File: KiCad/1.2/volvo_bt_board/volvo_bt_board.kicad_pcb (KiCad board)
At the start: 2 copper layers, 109.2 x 94 mm, 19 parts, among them J1 DB9_Male, J10 A_RX, J11 A_TX, J12 A_RST, J2 DAC_B, J3 DAC_A, J4 SF0, J5 SF1, J6 12V, J7 GND, J8 GND, J9 5V, U1 ESP32-DEVKITC-32D

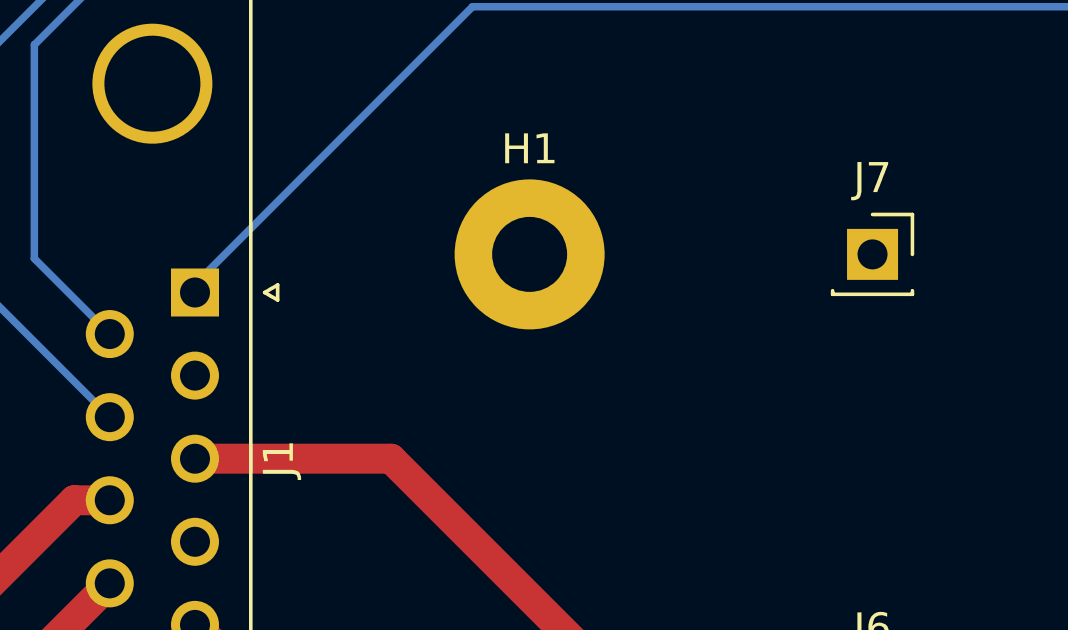
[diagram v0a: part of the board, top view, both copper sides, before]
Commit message: Add support for fast forward and reverse
 - Add support for scanmode (not tested)
 - Add ack bytes for approriate commands
 - Add board version 1.2
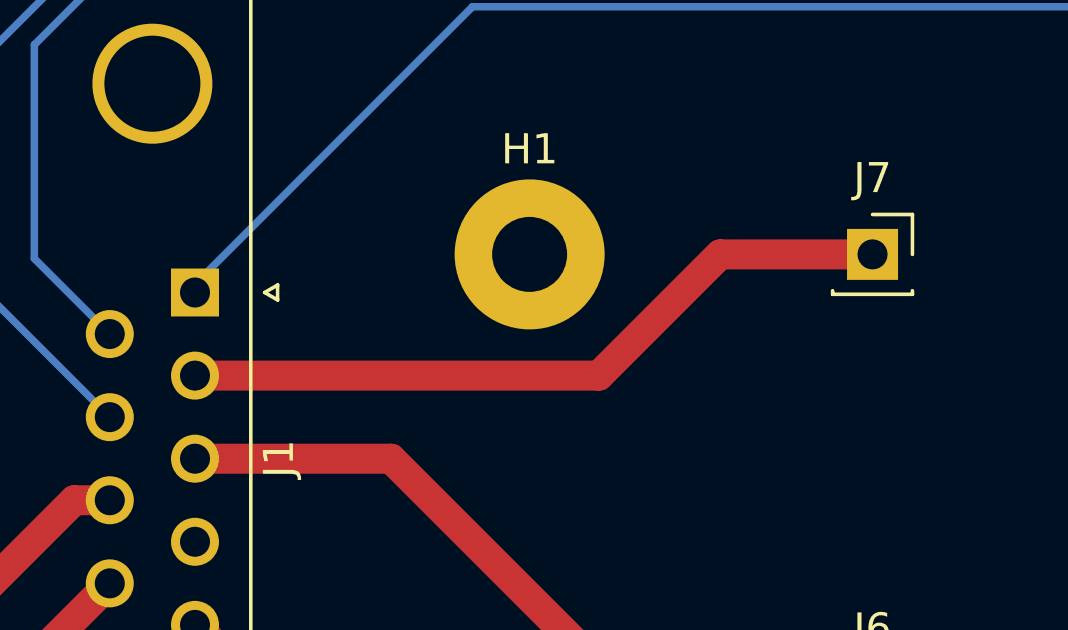
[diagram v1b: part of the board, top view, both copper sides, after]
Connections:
- J1 pad 2: GND -> GND_12V
- J7 pad 1: GND -> GND_12V
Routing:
- net GND_12V: track 0.00 -> 24.3 mm
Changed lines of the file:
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@@
       (layerselection 0x00010fc_ffffffff)
       (disableapertmacros false)
-      (usegerberextensions true)
-      (usegerberattributes false)
-      (usegerberadvancedattributes false)
-      (creategerberjobfile false)
+      (usegerberextensions false)
+      (usegerberattributes true)
+      (usegerberadvancedattributes true)
+      (creategerberjobfile true)
       (svguseinch false)
       (svgprecision 6)
@@
       (psa4output false)
       (plotreference true)
-      (plotvalue false)
+      (plotvalue true)
       (plotinvisibletext false)
       (sketchpadsonfab false)
-      (subtractmaskfromsilk true)
+      (subtractmaskfromsilk false)
       (outputformat 1)
       (mirror false)
       (drillshape 0)
       (scaleselection 1)
-      (outputdirectory "./jlcpcb-gerbers/")
+      (outputdirectory "./")
     )
   )
@@
   (net 76 "ARDUINO_RESET")
   (net 77 "Net-(J12-Pad1)")
+  (net 78 "GND_12V")
   (footprint "MountingHole:MountingHole_2.5mm_Pad" (layer "F.Cu")
     (at 144.78 132.08)
@@
     (fp_line (start -1.27 1.27) (end -1.27 -1.27) (layer "F.Fab") (width 0.1))
     (pad "1" thru_hole rect locked (at 0 0) (size 1.7 1.7) (drill 1) (layers *.Cu *.Mask)
-      (net 56 "GND") (pinfunction "Pin_1") (pintype "passive"))
+      (net 78 "GND_12V") (pinfunction "Pin_1") (pintype "passive"))
     (model "${KICAD6_3DMODEL_DIR}/Connector_PinSocket_2.54mm.3dshapes/PinSocket_1x01_P2.54mm_Vertical.wrl"
       (offset (xyz 0 0 0))
@@
       (net 55 "MELBUS_CLK") (pinfunction "1") (pintype "passive"))
     (pad "2" thru_hole circle locked (at 2.77 0 270) (size 1.6 1.6) (drill 1) (layers *.Cu *.Mask)
-      (net 56 "GND") (pinfunction "2") (pintype "passive"))
+      (net 78 "GND_12V") (pinfunction "2") (pintype "passive"))
     (pad "3" thru_hole circle locked (at 5.54 0 270) (size 1.6 1.6) (drill 1) (layers *.Cu *.Mask)
       (net 71 "12V") (pinfunction "3") (pintype "passive"))
@@
   (segment locked (start 135.18 114.86) (end 135.255 114.935) (width 0.25) (layer "F.Cu") (net 77))
   (segment locked (start 135.18 114.86) (end 135.255 114.935) (width 1) (layer "B.Cu") (net 77))
+  (segment (start 95.655 61.825) (end 99.695 57.785) (width 1) (layer "F.Cu") (net 78))
+  (segment (start 99.695 57.785) (end 104.775 57.785) (width 1) (layer "F.Cu") (net 78))
+  (segment (start 82.190331 61.825) (end 95.655 61.825) (width 1) (layer "F.Cu") (net 78))
   (zone locked (net 56) (net_name "GND") (layer "F.Cu") (hatch edge 0.508)
     (connect_pads (clearance 0.508))
